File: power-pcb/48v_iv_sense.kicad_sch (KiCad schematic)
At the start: 24 parts, among them J8 Screw_Terminal_01x03, U10 INA240A1D, U11 ADS1015IDGS, U12 ISO1540

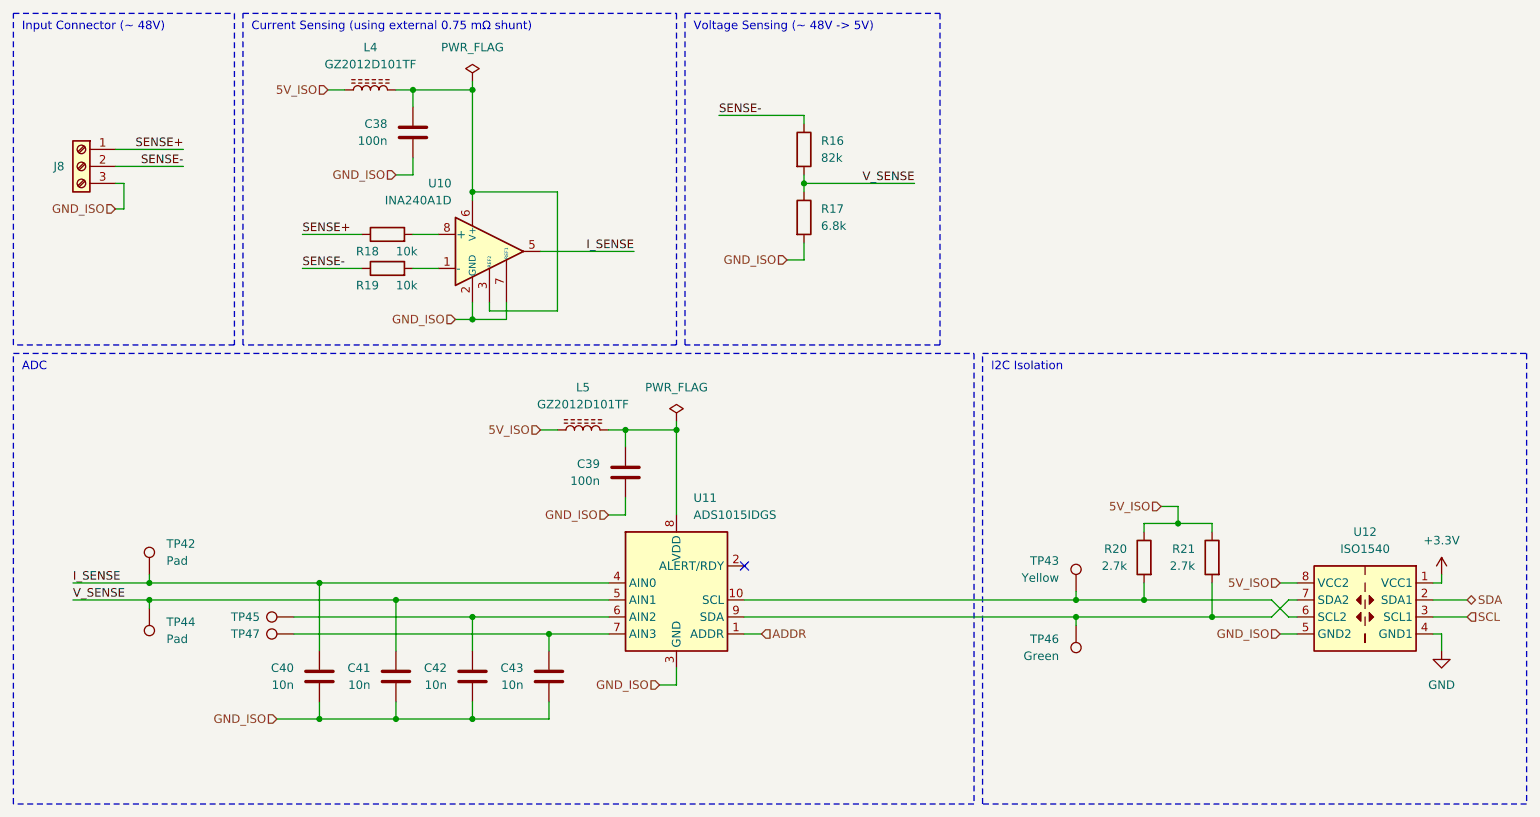
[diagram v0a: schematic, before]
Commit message: power-pcb: re-annotate schematic and start board
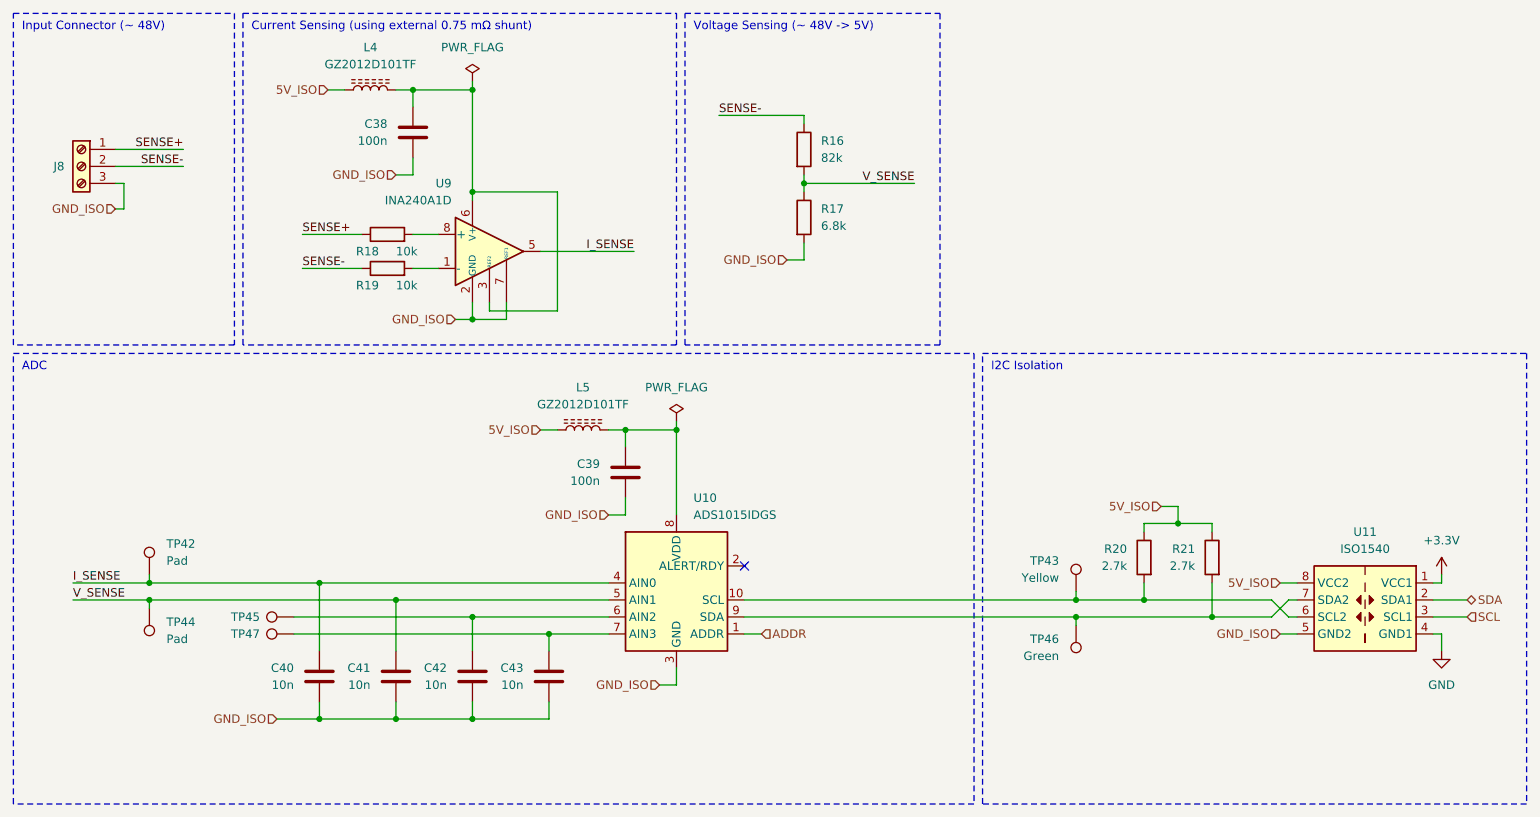
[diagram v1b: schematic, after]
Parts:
- renumbered U11 to U10, U12 to U11, U10 to U9
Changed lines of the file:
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@@
 		(in_pos_files yes)
 		(dnp no)
-		(property "Reference" "U10"
+		(property "Reference" "U9"
 			(at 78.1619 38.1 0)
 			(show_name no)
@@
 			(project "power-pcb"
 				(path "/4b4cf3aa-c94c-4150-b9c5-35049cd71136/50636587-2815-4d8e-b0bd-5f3d88757853/3693d20b-149d-45d7-af15-a350745d6368"
-					(reference "U13")
+					(reference "U12")
 					(unit 1)
 					(variant
@@
 				)
 				(path "/4b4cf3aa-c94c-4150-b9c5-35049cd71136/50636587-2815-4d8e-b0bd-5f3d88757853/82c46a0b-eb43-4701-b45e-f82f376cbba5"
-					(reference "U10")
+					(reference "U9")
 					(unit 1)
 					(variant
@@
 		(in_pos_files yes)
 		(dnp no)
-		(property "Reference" "U11"
+		(property "Reference" "U10"
 			(at 114.3 85.09 0)
 			(show_name no)
@@
 			(project "power-pcb"
 				(path "/4b4cf3aa-c94c-4150-b9c5-35049cd71136/50636587-2815-4d8e-b0bd-5f3d88757853/3693d20b-149d-45d7-af15-a350745d6368"
-					(reference "U14")
+					(reference "U13")
 					(unit 1)
 					(variant
@@
 				)
 				(path "/4b4cf3aa-c94c-4150-b9c5-35049cd71136/50636587-2815-4d8e-b0bd-5f3d88757853/82c46a0b-eb43-4701-b45e-f82f376cbba5"
-					(reference "U11")
+					(reference "U10")
 					(unit 1)
 					(variant
@@
 		(dnp no)
 		(fields_autoplaced yes)
-		(property "Reference" "U12"
+		(property "Reference" "U11"
 			(at 214.63 90.17 0)
 			(show_name no)
@@
 			(project "power-pcb"
 				(path "/4b4cf3aa-c94c-4150-b9c5-35049cd71136/50636587-2815-4d8e-b0bd-5f3d88757853/3693d20b-149d-45d7-af15-a350745d6368"
-					(reference "U15")
+					(reference "U14")
 					(unit 1)
 					(variant
@@
 				)
 				(path "/4b4cf3aa-c94c-4150-b9c5-35049cd71136/50636587-2815-4d8e-b0bd-5f3d88757853/82c46a0b-eb43-4701-b45e-f82f376cbba5"
-					(reference "U12")
-					(unit 1)
-					(variant
+					(reference "U11")
+					(unit 1)
+					(variant

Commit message: power-pcb: fix schematic after review
- Add footprint for resitive load for the RECOM
- Add Opamps when useful
- Add capacitor and change some footprint sizes
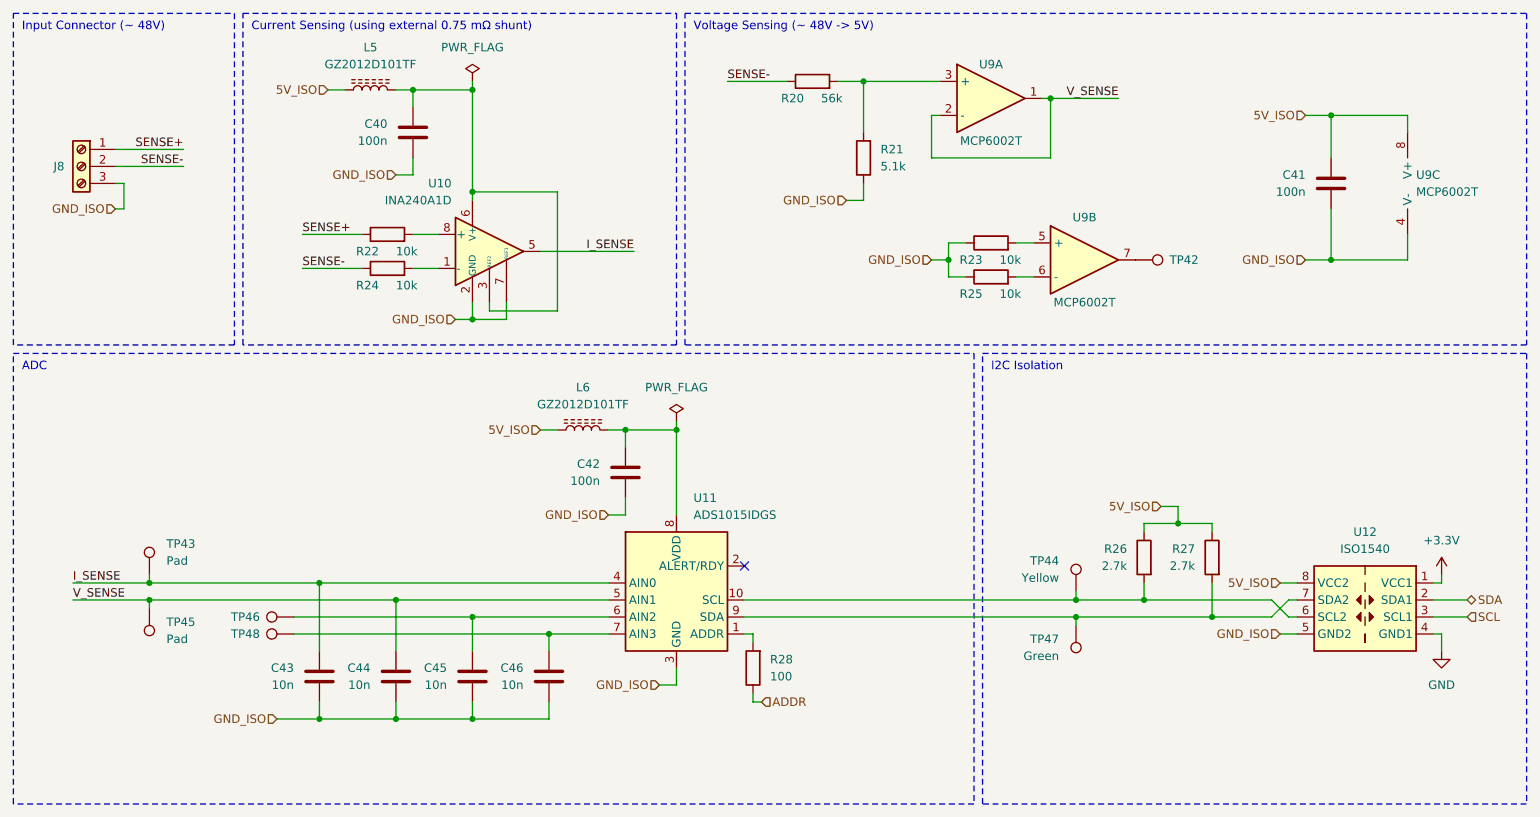
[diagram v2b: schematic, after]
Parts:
- removed R16: 82k, Resistor_SMD:R_0603_1608Metric_Pad0.98x0.95mm_HandSolder, symbol Device:R
- removed R17: 6.8k, Resistor_SMD:R_0603_1608Metric_Pad0.98x0.95mm_HandSolder, symbol Device:R
- added C41: 100n, Capacitor_SMD:C_0402_1005Metric_Pad0.74x0.62mm_HandSolder, symbol Device:C
- added R20: 56k, Resistor_SMD:R_0603_1608Metric_Pad0.98x0.95mm_HandSolder, symbol Device:R
- added R21: 5.1k, Resistor_SMD:R_0402_1005Metric_Pad0.72x0.64mm_HandSolder, symbol Device:R
- added R23, R25: 10k, Resistor_SMD:R_0603_1608Metric_Pad0.98x0.95mm_HandSolder, symbol Device:R
- added R28: 100, Resistor_SMD:R_0603_1608Metric_Pad0.98x0.95mm_HandSolder, symbol Device:R
- added TP42: Hole, TestPoint:TestPoint_THTPad_D2.0mm_Drill1.0mm, symbol Connector:TestPoint
- added U9: MCP6002T, Package_SO:SOIC-8_3.9x4.9mm_P1.27mm, symbol Device:Opamp_Dual
- C40: renamed from C38; footprint Capacitor_SMD:C_0603_1608Metric_Pad1.08x0.95mm_HandSolder -> Capacitor_SMD:C_0402_1005Metric_Pad0.74x0.62mm_HandSolder; JLCPCB C14663 -> C307331
- C42: renamed from C39; footprint Capacitor_SMD:C_0603_1608Metric_Pad1.08x0.95mm_HandSolder -> Capacitor_SMD:C_0402_1005Metric_Pad0.74x0.62mm_HandSolder; JLCPCB C14663 -> C307331
- renumbered C40 to C43, C41 to C44, C42 to C45, C43 to C46, L4 to L5, L5 to L6, R18 to R22, R19 to R24, R20 to R26, R21 to R27, TP42 to TP43, TP43 to TP44, TP44 to TP45, TP45 to TP46, TP46 to TP47, TP47 to TP48, U9 to U10, U10 to U11, U11 to U12
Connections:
- net 5V_ISO: now also C41.1, U9.8 (V+)
- net ADDR: now also R28.1; no longer U11.1 (ADDR)
- net GND_ISO: now also C41.2, R21.1, R23.1, R25.1, U9.4 (V-)
- net SENSE-: now also R20.1
- net V_SENSE: now also U9.1, U9.2 (-)
- new net: R23.2, U9.5 (+)
- new net: R25.2, U9.6 (-)
- new net: TP42.1, U9.7
- new net: R20.2, R21.2, U9.3 (+)
- new net: R28.2, U11.1 (ADDR)

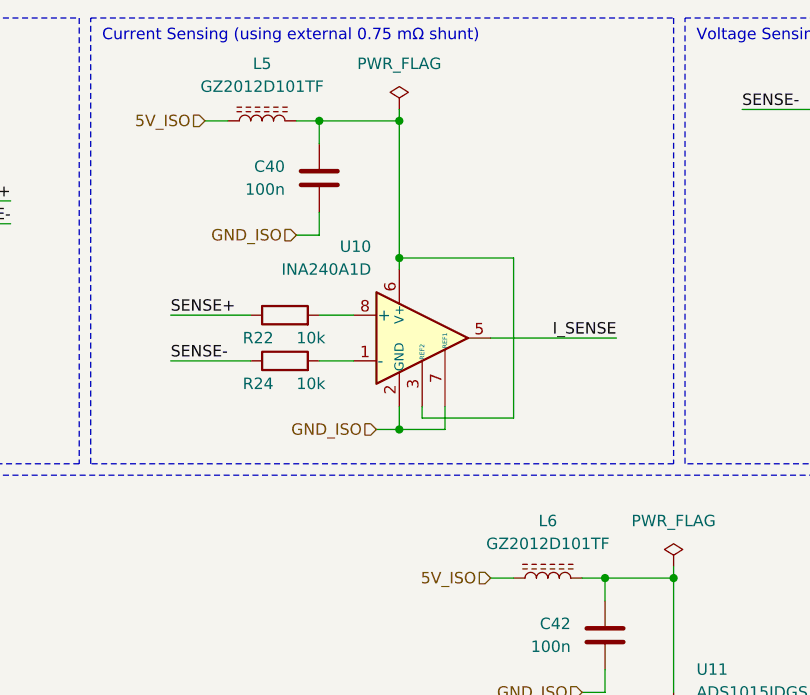
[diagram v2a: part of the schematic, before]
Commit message: power-pcb: work on part placement and JLCPCB DNP
Some of the components that were recentlt added had not been marked as
DNP for JLCPCB yet, this is now done.
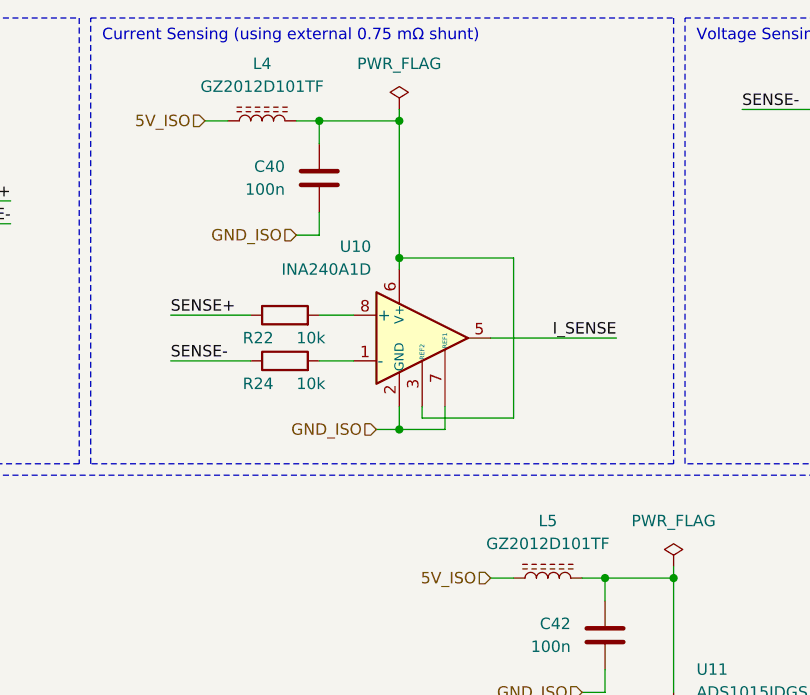
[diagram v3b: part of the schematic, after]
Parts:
- renumbered L5 to L4, L6 to L5
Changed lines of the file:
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@@
 					(reference "U13")
 					(unit 2)
+					(variant
+						(name "JLCPCB")
+					)
 				)
 				(path "/4b4cf3aa-c94c-4150-b9c5-35049cd71136/50636587-2815-4d8e-b0bd-5f3d88757853/82c46a0b-eb43-4701-b45e-f82f376cbba5"
 					(reference "U9")
 					(unit 2)
+					(variant
+						(name "JLCPCB")
+					)
 				)
 			)
@@
 					(reference "R30")
 					(unit 1)
+					(variant
+						(name "JLCPCB")
+					)
 				)
 				(path "/4b4cf3aa-c94c-4150-b9c5-35049cd71136/50636587-2815-4d8e-b0bd-5f3d88757853/82c46a0b-eb43-4701-b45e-f82f376cbba5"
 					(reference "R21")
 					(unit 1)
+					(variant
+						(name "JLCPCB")
+					)
 				)
 			)
@@
 					(reference "U13")
 					(unit 1)
+					(variant
+						(name "JLCPCB")
+					)
 				)
 				(path "/4b4cf3aa-c94c-4150-b9c5-35049cd71136/50636587-2815-4d8e-b0bd-5f3d88757853/82c46a0b-eb43-4701-b45e-f82f376cbba5"
 					(reference "U9")
 					(unit 1)
+					(variant
+						(name "JLCPCB")
+					)
 				)
 			)
@@
 		(dnp no)
 		(fields_autoplaced yes)
-		(property "Reference" "L5"
+		(property "Reference" "L4"
 			(at 66.04 17.78 90)
 			(show_name no)
@@
 			(project "power-pcb"
 				(path "/4b4cf3aa-c94c-4150-b9c5-35049cd71136/50636587-2815-4d8e-b0bd-5f3d88757853/3693d20b-149d-45d7-af15-a350745d6368"
-					(reference "L7")
+					(reference "L6")
 					(unit 1)
 					(variant
@@
 				)
 				(path "/4b4cf3aa-c94c-4150-b9c5-35049cd71136/50636587-2815-4d8e-b0bd-5f3d88757853/82c46a0b-eb43-4701-b45e-f82f376cbba5"
-					(reference "L5")
+					(reference "L4")
 					(unit 1)
 					(variant
@@
 					(reference "U13")
 					(unit 3)
+					(variant
+						(name "JLCPCB")
+					)
 				)
 				(path "/4b4cf3aa-c94c-4150-b9c5-35049cd71136/50636587-2815-4d8e-b0bd-5f3d88757853/82c46a0b-eb43-4701-b45e-f82f376cbba5"
 					(reference "U9")
 					(unit 3)
+					(variant
+						(name "JLCPCB")
+					)
 				)
 			)
@@
 					(reference "R29")
 					(unit 1)
+					(variant
+						(name "JLCPCB")
+					)
 				)
 				(path "/4b4cf3aa-c94c-4150-b9c5-35049cd71136/50636587-2815-4d8e-b0bd-5f3d88757853/82c46a0b-eb43-4701-b45e-f82f376cbba5"
 					(reference "R20")
 					(unit 1)
+					(variant
+						(name "JLCPCB")
+					)
 				)
 			)
@@
 					(reference "R37")
 					(unit 1)
+					(variant
+						(name "JLCPCB")
+					)
 				)
 				(path "/4b4cf3aa-c94c-4150-b9c5-35049cd71136/50636587-2815-4d8e-b0bd-5f3d88757853/82c46a0b-eb43-4701-b45e-f82f376cbba5"
 					(reference "R28")
 					(unit 1)
+					(variant
+						(name "JLCPCB")
+					)
 				)
 			)
@@
 		(dnp no)
 		(fields_autoplaced yes)
-		(property "Reference" "L6"
+		(property "Reference" "L5"
 			(at 97.79 68.58 90)
 			(show_name no)
@@
 			(project "power-pcb"
 				(path "/4b4cf3aa-c94c-4150-b9c5-35049cd71136/50636587-2815-4d8e-b0bd-5f3d88757853/3693d20b-149d-45d7-af15-a350745d6368"
-					(reference "L8")
+					(reference "L7")
 					(unit 1)
 					(variant
@@
 				)
 				(path "/4b4cf3aa-c94c-4150-b9c5-35049cd71136/50636587-2815-4d8e-b0bd-5f3d88757853/82c46a0b-eb43-4701-b45e-f82f376cbba5"
-					(reference "L6")
+					(reference "L5")
 					(unit 1)
 					(variant

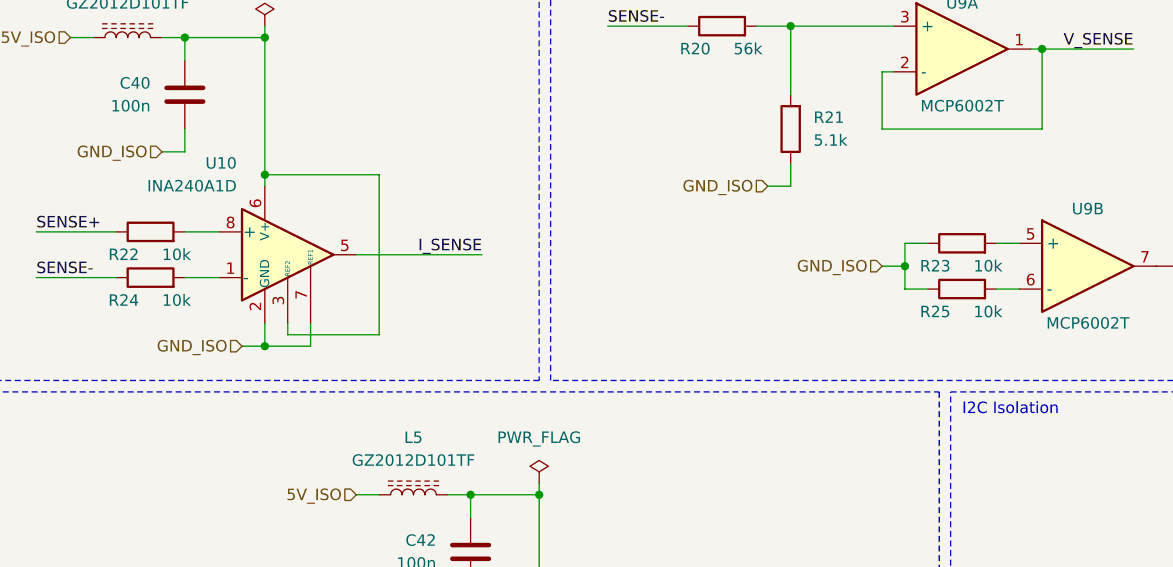
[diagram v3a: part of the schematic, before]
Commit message: power-pcb: change some 10k to 12k
JLCPCB doesn't offer a small package for the 10k resistors so some had
to be changed.
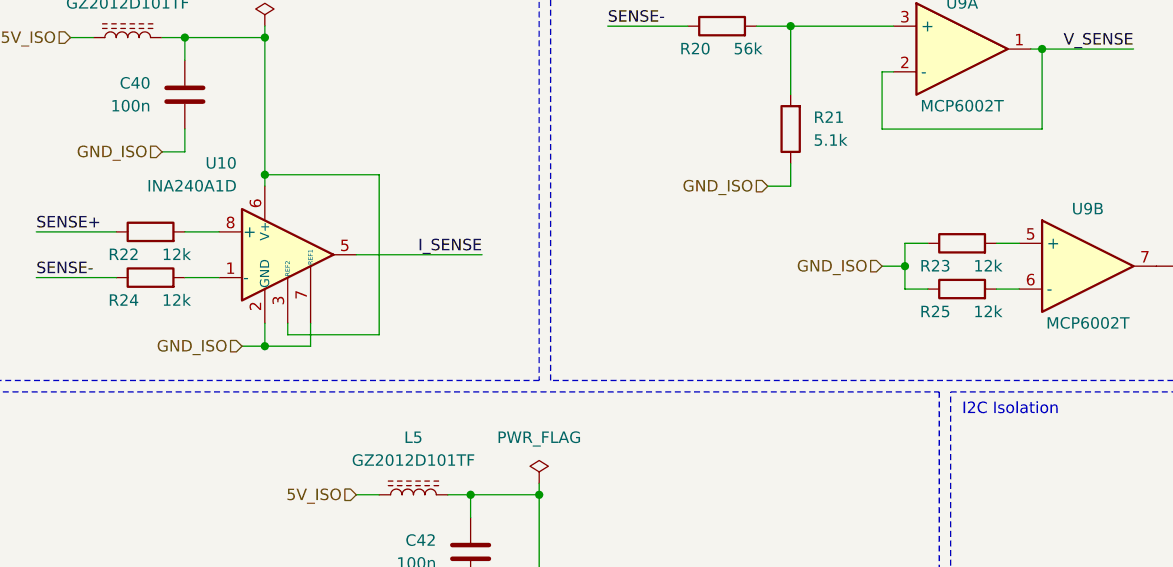
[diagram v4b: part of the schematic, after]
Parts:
- R22, R23, R24, R25: value 10k -> 12k
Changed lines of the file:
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@@
 	(title_block
 		(title "48V Battery I-V Sensing")
-		(date "2026-06-13")
+		(date "2026-06-19")
 		(rev "v1.1.0")
 	)
@@
 			)
 		)
-		(property "Value" "10k"
+		(property "Value" "12k"
 			(at 69.85 53.34 90)
 			(show_name no)
@@
 			)
 		)
-		(property "Value" "10k"
+		(property "Value" "12k"
 			(at 160.02 54.61 90)
 			(show_name no)
@@
 			)
 		)
-		(property "Value" "10k"
+		(property "Value" "12k"
 			(at 69.85 48.26 90)
 			(show_name no)
@@
 			)
 		)
-		(property "Value" "10k"
+		(property "Value" "12k"
 			(at 160.02 49.53 90)
 			(show_name no)

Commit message: power-pcb: finish placement and started routing
Started routing power traces only and didn't place test points yet.
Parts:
- R22, R23, R24, R25: footprint Resistor_SMD:R_0603_1608Metric_Pad0.98x0.95mm_HandSolder -> Resistor_SMD:R_0402_1005Metric_Pad0.72x0.64mm_HandSolder; JLCPCB C25804 -> C25752
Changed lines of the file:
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@@
 			)
 		)
-		(property "Footprint" "Resistor_SMD:R_0603_1608Metric_Pad0.98x0.95mm_HandSolder"
+		(property "Footprint" "Resistor_SMD:R_0402_1005Metric_Pad0.72x0.64mm_HandSolder"
 			(at 68.58 52.578 90)
 			(hide yes)
@@
 			)
 		)
-		(property "JLCPCB" "C25804"
+		(property "JLCPCB" "C25752"
 			(at 68.58 50.8 90)
 			(hide yes)
@@
 			)
 		)
-		(property "Footprint" "Resistor_SMD:R_0603_1608Metric_Pad0.98x0.95mm_HandSolder"
+		(property "Footprint" "Resistor_SMD:R_0402_1005Metric_Pad0.72x0.64mm_HandSolder"
 			(at 158.75 53.848 90)
 			(hide yes)
@@
 			)
 		)
-		(property "JLCPCB" "C25804"
+		(property "JLCPCB" "C25752"
 			(at 158.75 52.07 90)
 			(hide yes)
@@
 			)
 		)
-		(property "Footprint" "Resistor_SMD:R_0603_1608Metric_Pad0.98x0.95mm_HandSolder"
+		(property "Footprint" "Resistor_SMD:R_0402_1005Metric_Pad0.72x0.64mm_HandSolder"
 			(at 68.58 47.498 90)
 			(hide yes)
@@
 			)
 		)
-		(property "JLCPCB" "C25804"
+		(property "JLCPCB" "C25752"
 			(at 68.58 45.72 90)
 			(hide yes)
@@
 			)
 		)
-		(property "Footprint" "Resistor_SMD:R_0603_1608Metric_Pad0.98x0.95mm_HandSolder"
+		(property "Footprint" "Resistor_SMD:R_0402_1005Metric_Pad0.72x0.64mm_HandSolder"
 			(at 158.75 48.768 90)
 			(hide yes)
@@
 			)
 		)
-		(property "JLCPCB" "C25804"
+		(property "JLCPCB" "C25752"
 			(at 158.75 46.99 90)
 			(hide yes)
